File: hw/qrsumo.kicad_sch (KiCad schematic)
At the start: 76 parts, among them J1 Conn_01x02, J2 USB_B_Micro, J3 UART, J4 MOTOR_LEFT, J5 MOTOR_RIGHT, J6 Conn_01x07, J7 Conn_01x07, J8 VBAT, Q1 AO3400A, Q2 DMG2301L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

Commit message: adding first layout
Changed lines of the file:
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@@
   (junction (at 279.4 193.675) (diameter 0) (color 0 0 0 0)
   )
-  (junction (at 70.485 53.34) (diameter 0) (color 0 0 0 0)
-  )
   (junction (at 74.295 203.835) (diameter 0) (color 0 0 0 0)
   )
@@
     (stroke (width 0) (type default) (color 0 0 0 0))
   )
-  (wire (pts (xy 70.485 53.34) (xy 81.915 53.34))
+  (wire (pts (xy 64.135 53.34) (xy 81.915 53.34))
     (stroke (width 0) (type default) (color 0 0 0 0))
   )
@@
     (stroke (width 0) (type default) (color 0 0 0 0))
   )
-  (wire (pts (xy 64.135 53.34) (xy 70.485 53.34))
-    (stroke (width 0) (type default) (color 0 0 0 0))
-  )
   (wire (pts (xy 228.6 252.73) (xy 267.335 252.73))
     (stroke (width 0) (type default) (color 0 0 0 0))
@@
     (stroke (width 0) (type default) (color 0 0 0 0))
   )
+  (wire (pts (xy 49.53 88.265) (xy 49.53 90.17))
+    (stroke (width 0) (type default) (color 0 0 0 0))
+  )
   (wire (pts (xy 64.135 29.21) (xy 64.135 36.83))
     (stroke (width 0) (type default) (color 0 0 0 0))
@@
     (stroke (width 0) (type default) (color 0 0 0 0))
   )
-  (wire (pts (xy 49.53 88.265) (xy 49.53 90.17))
-    (stroke (width 0) (type default) (color 0 0 0 0))
-  )
   (wire (pts (xy 132.715 59.055) (xy 132.715 62.23))
     (stroke (width 0) (type default) (color 0 0 0 0))
@@
     (pin "1")
   )
-  (symbol (lib_id "power:PWR_FLAG") (at 70.485 53.34 0) (unit 1)
-    (in_bom yes) (on_board yes) (fields_autoplaced)
-    (property "Reference" "#FLG0101" (id 0) (at 70.485 51.435 0)
-      (effects (font (size 1.27 1.27)) hide)
-    )
-    (property "Value" "PWR_FLAG" (id 1) (at 70.485 48.26 0)
-      (effects (font (size 1.27 1.27)) hide)
-    )
-    (property "Footprint" "" (id 2) (at 70.485 53.34 0)
-      (effects (font (size 1.27 1.27)) hide)
-    )
-    (property "Datasheet" "~" (id 3) (at 70.485 53.34 0)
-      (effects (font (size 1.27 1.27)) hide)
-    )
-    (pin "1")
-  )
   (symbol (lib_id "Connector_Generic:Conn_01x02") (at 317.5 185.42 0) (unit 1)
     (in_bom yes) (on_board yes) (fields_autoplaced)
@@
   (symbol (lib_id "Device:D_Photo") (at 49.53 95.25 270) (unit 1)
     (in_bom yes) (on_board yes) (fields_autoplaced)
-    (property "Reference" "D6" (id 0) (at 53.975 93.0274 90)
+    (property "Reference" "D6" (id 0) (at 54.61 93.0274 90)
       (effects (font (size 1.27 1.27)) (justify left))
     )
-    (property "Value" "D_Photo" (id 1) (at 53.975 95.5674 90)
+    (property "Value" "D_Photo" (id 1) (at 54.61 95.5674 90)
       (effects (font (size 1.27 1.27)) (justify left))
     )
@@
   )
   (symbol_instances
-    (path "/092611c4-bcf2-40a3-8148-66dd688d1de7"
-      (reference "#FLG0101") (unit 1) (value "PWR_FLAG") (footprint "")
-    )
     (path "/d7d6246e-64b5-41cf-8ccc-f0896cb30cb0"
       (reference "#FLG0102") (unit 1) (value "PWR_FLAG") (footprint "")

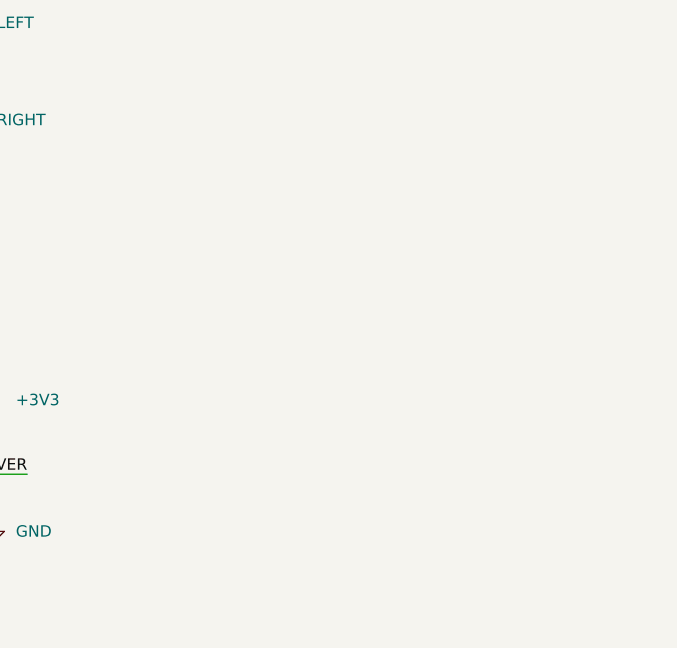
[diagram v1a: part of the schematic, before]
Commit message: Improve placement, fix footprints
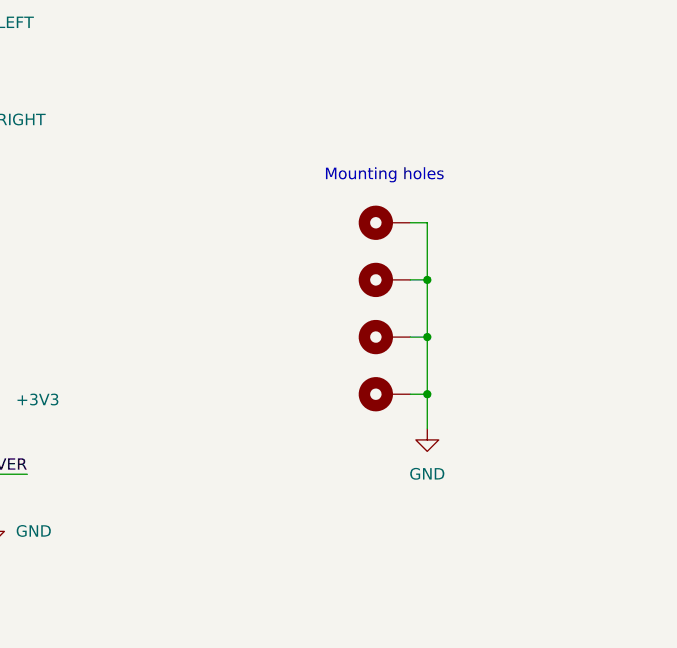
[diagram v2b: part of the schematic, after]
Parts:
- added H1, H2, H3, H4: MountingHole_Pad, MountingHole:MountingHole_2.7mm_M2.5_Pad_Via, symbol Mechanical:MountingHole_Pad
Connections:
- net GND: now also H1.1, H2.1, H3.1, H4.1
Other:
- note added: "Mounting holes"
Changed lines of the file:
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@@
   (junction (at 54.61 211.455) (diameter 0) (color 0 0 0 0)
   )
+  (junction (at 375.285 205.74) (diameter 0) (color 0 0 0 0)
+  )
   (junction (at 203.835 23.495) (diameter 0) (color 0 0 0 0)
   )
@@
   (junction (at 109.22 243.84) (diameter 0) (color 0 0 0 0)
   )
+  (junction (at 375.285 212.09) (diameter 0) (color 0 0 0 0)
+  )
   (junction (at 367.665 85.09) (diameter 0) (color 0 0 0 0)
   )
@@
   (junction (at 194.31 23.495) (diameter 0) (color 0 0 0 0)
   )
+  (junction (at 375.285 218.44) (diameter 0) (color 0 0 0 0)
+  )
   (junction (at 224.155 257.175) (diameter 0) (color 0 0 0 0)
   )
@@
     (stroke (width 0) (type default) (color 0 0 0 0))
   )
+  (wire (pts (xy 375.285 205.74) (xy 375.285 212.09))
+    (stroke (width 0) (type default) (color 0 0 0 0))
+  )
   (wire (pts (xy 156.845 66.675) (xy 165.1 66.675))
     (stroke (width 0) (type default) (color 0 0 0 0))
@@
     (stroke (width 0) (type default) (color 0 0 0 0))
   )
+  (wire (pts (xy 373.38 199.39) (xy 375.285 199.39))
+    (stroke (width 0) (type default) (color 0 0 0 0))
+  )
   (wire (pts (xy 257.175 239.395) (xy 257.175 240.665))
     (stroke (width 0) (type default) (color 0 0 0 0))
@@
     (stroke (width 0) (type default) (color 0 0 0 0))
   )
+  (wire (pts (xy 375.285 218.44) (xy 375.285 222.25))
+    (stroke (width 0) (type default) (color 0 0 0 0))
+  )
   (wire (pts (xy 125.73 239.395) (xy 125.73 243.84))
     (stroke (width 0) (type default) (color 0 0 0 0))
@@
     (stroke (width 0) (type default) (color 0 0 0 0))
   )
+  (wire (pts (xy 375.285 199.39) (xy 375.285 205.74))
+    (stroke (width 0) (type default) (color 0 0 0 0))
+  )
   (wire (pts (xy 180.975 224.79) (xy 180.975 216.535))
     (stroke (width 0) (type default) (color 0 0 0 0))
@@
     (stroke (width 0) (type default) (color 0 0 0 0))
   )
+  (wire (pts (xy 373.38 212.09) (xy 375.285 212.09))
+    (stroke (width 0) (type default) (color 0 0 0 0))
+  )
   (wire (pts (xy 54.61 156.21) (xy 54.61 157.48))
     (stroke (width 0) (type default) (color 0 0 0 0))
@@
     (stroke (width 0) (type default) (color 0 0 0 0))
   )
+  (wire (pts (xy 373.38 205.74) (xy 375.285 205.74))
+    (stroke (width 0) (type default) (color 0 0 0 0))
+  )
   (wire (pts (xy 54.61 206.375) (xy 54.61 211.455))
     (stroke (width 0) (type default) (color 0 0 0 0))
@@
     (stroke (width 0) (type default) (color 0 0 0 0))
   )
+  (wire (pts (xy 375.285 212.09) (xy 375.285 218.44))
+    (stroke (width 0) (type default) (color 0 0 0 0))
+  )
   (wire (pts (xy 156.845 26.035) (xy 156.845 31.115))
     (stroke (width 0) (type default) (color 0 0 0 0))
@@
     (stroke (width 0) (type default) (color 0 0 0 0))
   )
+  (wire (pts (xy 373.38 218.44) (xy 375.285 218.44))
+    (stroke (width 0) (type default) (color 0 0 0 0))
+  )
   (wire (pts (xy 257.175 225.425) (xy 257.175 217.17))
     (stroke (width 0) (type default) (color 0 0 0 0))
@@
     (effects (font (size 1.27 1.27)) (justify left bottom))
   )
+  (text "Mounting holes" (at 363.855 194.945 0)
+    (effects (font (size 1.27 1.27)) (justify left bottom))
+  )
   (text "Bootstrap pins:\n\n• Chip boot mode - GPIO0 and GPIO46\n• VDD_SPI voltage - GPIO45\n• ROM messages printing - GPIO46\n• JTAG signal source - GPIO3\n\n \n\nBoot Mode\n\nSPI Boot - GPI0 = 1, GPIO46 = Any\n\nDownload Boot  -  GPI0 = 0, GPIO46 = 0\n\nInvalid -  GPI0 = 0, GPIO46 = 1"
     (at 294.64 104.14 0)
@@
     (pin "2")
   )
+  (symbol (lib_id "Mechanical:MountingHole_Pad") (at 370.84 199.39 90) (unit 1)
+    (in_bom yes) (on_board yes) (fields_autoplaced)
+    (property "Reference" "H1" (id 0) (at 369.57 194.31 90)
+      (effects (font (size 1.27 1.27)) hide)
+    )
+    (property "Value" "MountingHole_Pad" (id 1) (at 369.57 194.31 90)
+      (effects (font (size 1.27 1.27)) hide)
+    )
+    (property "Footprint" "MountingHole:MountingHole_2.7mm_M2.5_Pad_Via" (id 2) (at 370.84 199.39 0)
+      (effects (font (size 1.27 1.27)) hide)
+    )
+    (property "Datasheet" "~" (id 3) (at 370.84 199.39 0)
+      (effects (font (size 1.27 1.27)) hide)
+    )
+    (pin "1")
+  )
   (symbol (lib_id "power:GND") (at 121.92 62.23 0) (unit 1)
     (in_bom yes) (on_board yes) (fields_autoplaced)
@@
     (pin "1")
   )
+  (symbol (lib_id "Mechanical:MountingHole_Pad") (at 370.84 212.09 90) (unit 1)
+    (in_bom yes) (on_board yes) (fields_autoplaced)
+    (property "Reference" "H3" (id 0) (at 369.57 207.01 90)
+      (effects (font (size 1.27 1.27)) hide)
+    )
+    (property "Value" "MountingHole_Pad" (id 1) (at 369.57 207.01 90)
+      (effects (font (size 1.27 1.27)) hide)
+    )
+    (property "Footprint" "MountingHole:MountingHole_2.7mm_M2.5_Pad_Via" (id 2) (at 370.84 212.09 0)
+      (effects (font (size 1.27 1.27)) hide)
+    )
+    (property "Datasheet" "~" (id 3) (at 370.84 212.09 0)
+      (effects (font (size 1.27 1.27)) hide)
+    )
+    (pin "1")
+  )
   (symbol (lib_id "Device:C_Small") (at 278.765 149.225 0) (unit 1)
     (in_bom yes) (on_board yes) (fields_autoplaced)
@@
     (pin "2")
   )
+  (symbol (lib_id "Mechanical:MountingHole_Pad") (at 370.84 205.74 90) (unit 1)
+    (in_bom yes) (on_board yes)
+    (property "Reference" "H2" (id 0) (at 369.57 198.12 90)
+      (effects (font (size 1.27 1.27)) hide)
+    )
+    (property "Value" "MountingHole_Pad" (id 1) (at 369.57 200.66 90)
+      (effects (font (size 1.27 1.27)) hide)
+    )
+    (property "Footprint" "MountingHole:MountingHole_2.7mm_M2.5_Pad_Via" (id 2) (at 370.84 205.74 0)
+      (effects (font (size 1.27 1.27)) hide)
+    )
+    (property "Datasheet" "~" (id 3) (at 370.84 205.74 0)
+      (effects (font (size 1.27 1.27)) hide)
+    )
+    (pin "1")
+  )
   (symbol (lib_id "power:GND") (at 187.96 135.89 0) (unit 1)
     (in_bom yes) (on_board yes) (fields_autoplaced)
@@
     (pin "2")
   )
+  (symbol (lib_id "Mechanical:MountingHole_Pad") (at 370.84 218.44 90) (unit 1)
+    (in_bom yes) (on_board yes)
+    (property "Reference" "H4" (id 0) (at 369.57 210.82 90)
+      (effects (font (size 1.27 1.27)) hide)
+    )
+    (property "Value" "MountingHole_Pad" (id 1) (at 369.57 213.36 90)
+      (effects (font (size 1.27 1.27)) hide)
+    )
+    (property "Footprint" "MountingHole:MountingHole_2.7mm_M2.5_Pad_Via" (id 2) (at 370.84 218.44 0)
+      (effects (font (size 1.27 1.27)) hide)
+    )
+    (property "Datasheet" "~" (id 3) (at 370.84 218.44 0)
+      (effects (font (size 1.27 1.27)) hide)
+    )
+    (pin "1")
+  )
   (symbol (lib_id "power:+BATT") (at 377.825 132.08 0) (unit 1)
     (in_bom yes) (on_board yes)
@@
     (pin "2")
   )
+  (symbol (lib_id "power:GND") (at 375.285 222.25 0) (unit 1)
+    (in_bom yes) (on_board yes) (fields_autoplaced)
+    (property "Reference" "#PWR0159" (id 0) (at 375.285 228.6 0)
+      (effects (font (size 1.27 1.27)) hide)
+    )
+    (property "Value" "GND" (id 1) (at 375.285 227.33 0))
+    (property "Footprint" "" (id 2) (at 375.285 222.25 0)
+      (effects (font (size 1.27 1.27)) hide)
+    )
+    (property "Datasheet" "" (id 3) (at 375.285 222.25 0)
+      (effects (font (size 1.27 1.27)) hide)
+    )
+    (pin "1")
+  )
   (symbol (lib_id "Device:C_Small") (at 296.545 149.86 0) (unit 1)
     (in_bom yes) (on_board yes) (fields_autoplaced)
@@
       (reference "#PWR0158") (unit 1) (value "GND") (footprint "")
     )
+    (path "/f0c5053d-0ac4-42b5-95cc-07f8f2bec884"
+      (reference "#PWR0159") (unit 1) (value "GND") (footprint "")
+    )
     (path "/28b13304-8297-468b-8efc-2a55768c3e6d"
       (reference "C1") (unit 1) (value "4.7u") (footprint "Capacitor_SMD:C_0603_1608Metric")
@@
       (reference "D12") (unit 1) (value "WS2812B") (footprint "LED_SMD:LED_WS2812B_PLCC4_5.0x5.0mm_P3.2mm")
     )
+    (path "/2956da1f-ef0c-4683-a5b6-49c6eb17c04c"
+      (reference "H1") (unit 1) (value "MountingHole_Pad") (footprint "MountingHole:MountingHole_2.7mm_M2.5_Pad_Via")
+    )
+    (path "/c43966a6-db95-4810-a7cb-3d6fcacc2bc8"
+      (reference "H2") (unit 1) (value "MountingHole_Pad") (footprint "MountingHole:MountingHole_2.7mm_M2.5_Pad_Via")
+    )
+    (path "/73d28a96-01f8-4740-a499-912c5c5c33af"
+      (reference "H3") (unit 1) (value "MountingHole_Pad") (footprint "MountingHole:MountingHole_2.7mm_M2.5_Pad_Via")
+    )
+    (path "/e8484633-585b-4e49-8829-b768e3544ef2"
+      (reference "H4") (unit 1) (value "MountingHole_Pad") (footprint "MountingHole:MountingHole_2.7mm_M2.5_Pad_Via")
+    )
     (path "/dfd06b64-e8e9-41ea-935d-cc4d5a32a04a"
